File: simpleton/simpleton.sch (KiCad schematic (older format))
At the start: 78 parts

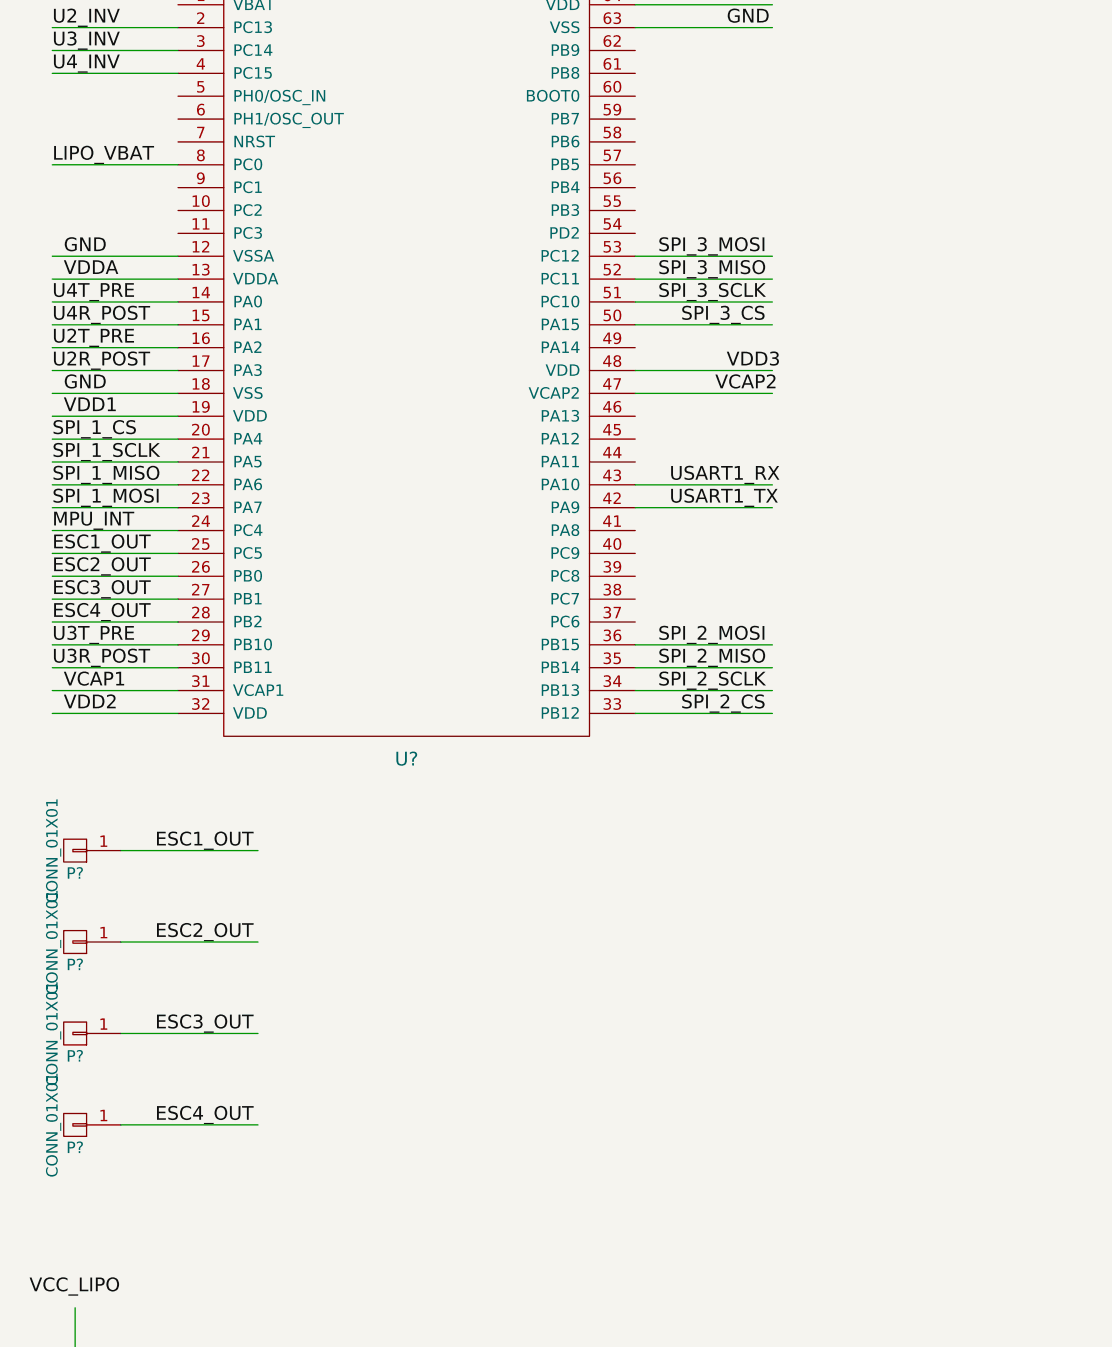
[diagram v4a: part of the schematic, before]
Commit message: Added buzzer
Closes #11
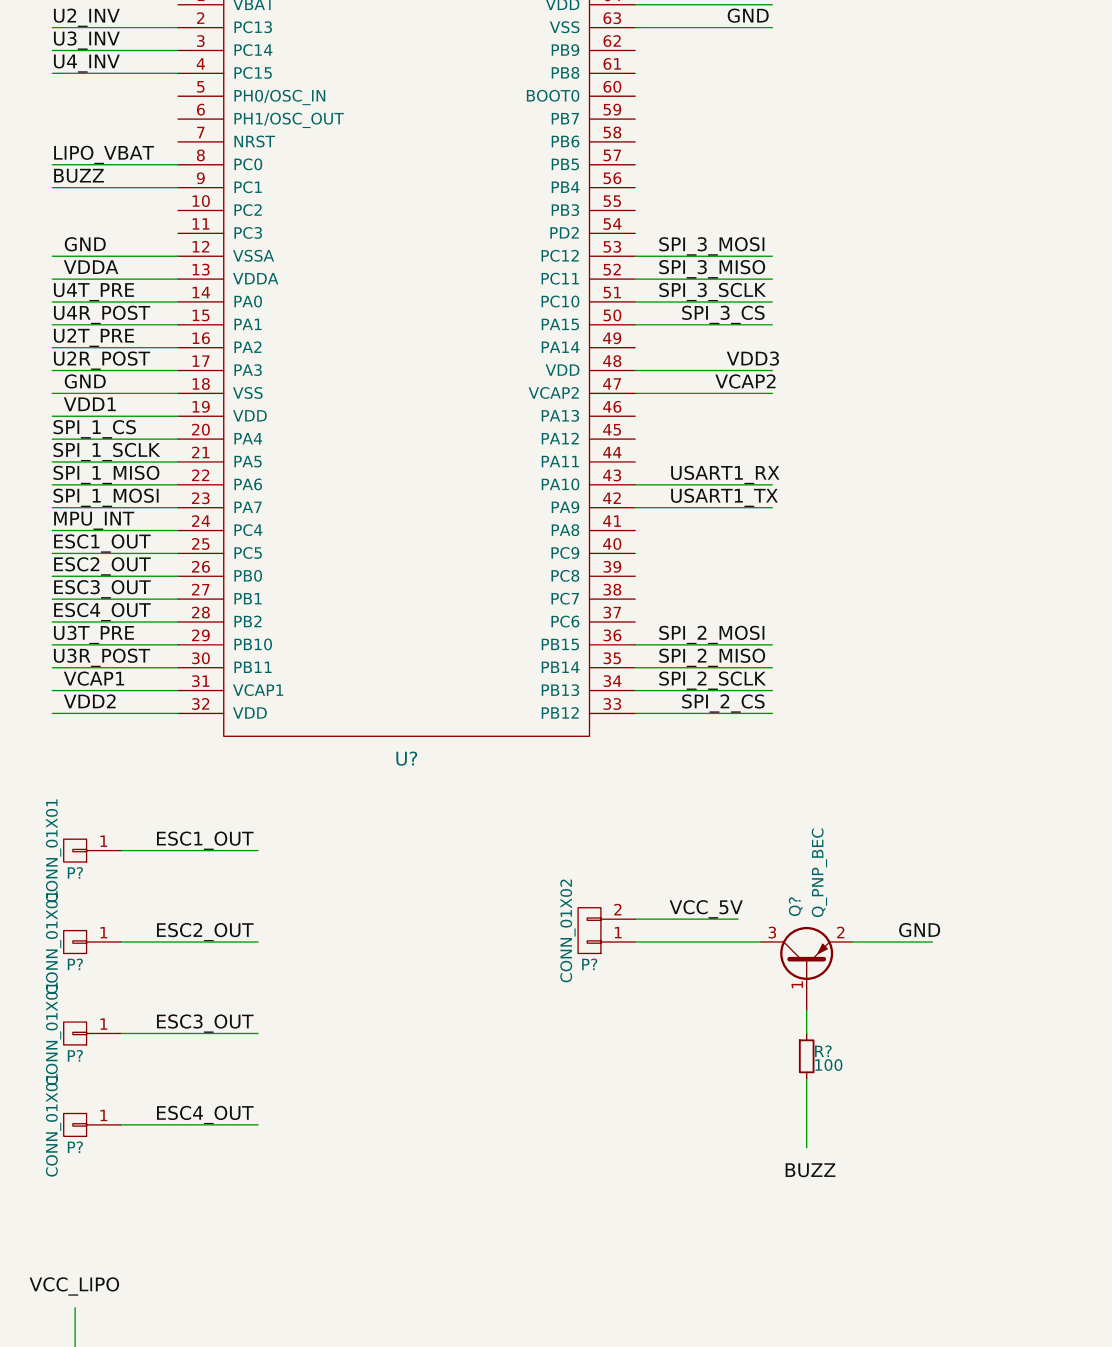
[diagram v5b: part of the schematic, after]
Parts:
- added P?: CONN_01X02, symbol CONN_01X02
- added Q?: Q_PNP_BEC, symbol Q_PNP_BEC
- added R?: 100, symbol R_Small
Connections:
- net labels added: BUZZ
- wire segments 281 -> 287

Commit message: Added status LEDS
Closes #4
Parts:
- added D? (x3): Led_Small, symbol Led_Small
- added R? (x3): 100, symbol R_Small
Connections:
- net labels added: LED1, LED2
- wire segments 287 -> 298
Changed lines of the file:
@@
 Text Label 800  2000 0    60   ~ 0
 BUZZ
+Wire Wire Line
+	2900 6800 2900 7000
+$Comp
+L Led_Small D?
+U 1 1 56D5A53F
+P 2900 7100
+F 0 "D?" H 2850 7225 50  0000 L CNN
+F 1 "Led_Small" H 2725 7000 50  0000 L CNN
+F 2 "" V 2900 7100 60  0000 C CNN
+F 3 "" V 2900 7100 60  0000 C CNN
+	1    2900 7100
+	0    -1   -1   0
+$EndComp
+Wire Wire Line
+	2900 7200 2900 7350
+$Comp
+L R_Small R?
+U 1 1 56D5A97A
+P 2900 7450
+F 0 "R?" H 2930 7470 50  0000 L CNN
+F 1 "100" H 2930 7410 50  0000 L CNN
+F 2 "" H 2900 7450 60  0000 C CNN
+F 3 "" H 2900 7450 60  0000 C CNN
+	1    2900 7450
+	1    0    0    -1
+$EndComp
+Wire Wire Line
+	2900 7550 2900 7700
+Text Label 2800 7800 0    60   ~ 0
+GND
+Text Label 2700 6750 0    60   ~ 0
+VCC_3_3V
+Wire Wire Line
+	3400 6800 3400 7000
+$Comp
+L Led_Small D?
+U 1 1 56D5B127
+P 3400 7100
+F 0 "D?" H 3350 7225 50  0000 L CNN
+F 1 "Led_Small" H 3225 7000 50  0000 L CNN
+F 2 "" V 3400 7100 60  0000 C CNN
+F 3 "" V 3400 7100 60  0000 C CNN
+	1    3400 7100
+	0    -1   -1   0
+$EndComp
+Wire Wire Line
+	3400 7200 3400 7350
+$Comp
+L R_Small R?
+U 1 1 56D5B12E
+P 3400 7450
+F 0 "R?" H 3430 7470 50  0000 L CNN
+F 1 "100" H 3430 7410 50  0000 L CNN
+F 2 "" H 3400 7450 60  0000 C CNN
+F 3 "" H 3400 7450 60  0000 C CNN
+	1    3400 7450
+	1    0    0    -1
+$EndComp
+Wire Wire Line
+	3400 7550 3400 7700
+Text Label 3300 7800 0    60   ~ 0
+LED1
+Text Label 3200 6750 0    60   ~ 0
+VCC_3_3V
+Wire Wire Line
+	3900 6800 3900 7000
+$Comp
+L Led_Small D?
+U 1 1 56D5B212
+P 3900 7100
+F 0 "D?" H 3850 7225 50  0000 L CNN
+F 1 "Led_Small" H 3725 7000 50  0000 L CNN
+F 2 "" V 3900 7100 60  0000 C CNN
+F 3 "" V 3900 7100 60  0000 C CNN
+	1    3900 7100
+	0    -1   -1   0
+$EndComp
+Wire Wire Line
+	3900 7200 3900 7350
+$Comp
+L R_Small R?
+U 1 1 56D5B219
+P 3900 7450
+F 0 "R?" H 3930 7470 50  0000 L CNN
+F 1 "100" H 3930 7410 50  0000 L CNN
+F 2 "" H 3900 7450 60  0000 C CNN
+F 3 "" H 3900 7450 60  0000 C CNN
+	1    3900 7450
+	1    0    0    -1
+$EndComp
+Wire Wire Line
+	3900 7550 3900 7700
+Text Label 3800 7800 0    60   ~ 0
+LED2
+Text Label 3700 6750 0    60   ~ 0
+VCC_3_3V
+Wire Wire Line
+	3350 1900 3950 1900
+Wire Wire Line
+	3350 1800 3950 1800
+Text Label 3750 1900 0    60   ~ 0
+LED1
+Text Label 3750 1800 0    60   ~ 0
+LED2
 $EndSCHEMATC

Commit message: Added boot loader support
Closes #14
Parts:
- added JP?: Jumper_NO_Small, symbol Jumper_NO_Small
- added R?: 10K, symbol R_Small
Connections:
- net labels added: BOOT0
- wire segments 298 -> 304
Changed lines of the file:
@@
 Text Label 1250 6100 0    60   ~ 0
-ESC4_OUT
-Text Label 800  3600 0    60   ~ 0
-ESC1_OUT
-Text Label 800  3700 0    60   ~ 0
-ESC2_OUT
-Text Label 800  3800 0    60   ~ 0
-ESC3_OUT
-Text Label 800  3900 0    60   ~ 0
 ESC4_OUT
 $Comp
@@
 	1100 6100 1700 6100
 Wire Wire Line
-	1350 3600 800  3600
-Wire Wire Line
-	1350 3700 800  3700
-Wire Wire Line
-	1350 3800 800  3800
-Wire Wire Line
 	1350 3900 800  3900
 Wire Wire Line
@@
 Text Label 3750 1800 0    60   ~ 0
 LED2
+Wire Wire Line
+	3350 3900 3950 3900
+Wire Wire Line
+	3350 3800 3950 3800
+Wire Wire Line
+	3350 3700 3950 3700
+Wire Wire Line
+	3350 3600 3950 3600
+Text Label 3500 3900 0    60   ~ 0
+ESC1_OUT
+Text Label 3500 3800 0    60   ~ 0
+ESC2_OUT
+Text Label 3500 3700 0    60   ~ 0
+ESC3_OUT
+Text Label 3500 3600 0    60   ~ 0
+ESC4_OUT
+Text Label 800  3900 0    60   ~ 0
+GND
+Wire Wire Line
+	3350 1600 3950 1600
+Text Label 3650 1600 0    60   ~ 0
+BOOT0
+Wire Wire Line
+	5550 4400 6250 4400
+Wire Wire Line
+	6000 4400 6000 4250
+Connection ~ 6000 4400
+$Comp
+L R_Small R?
+U 1 1 57133C31
+P 6350 4400
+F 0 "R?" H 6380 4420 50  0000 L CNN
+F 1 "10K" H 6380 4360 50  0000 L CNN
+F 2 "" H 6350 4400 60  0000 C CNN
+F 3 "" H 6350 4400 60  0000 C CNN
+	1    6350 4400
+	0    1    1    0
+$EndComp
+Wire Wire Line
+	6450 4400 6800 4400
+Text Label 6650 4400 0    60   ~ 0
+GND
+Text Label 5550 4400 0    60   ~ 0
+BOOT0
+$Comp
+L Jumper_NO_Small JP?
+U 1 1 5713413B
+P 6000 4150
+F 0 "JP?" H 6000 4230 50  0000 C CNN
+F 1 "Jumper_NO_Small" H 6010 4090 50  0001 C CNN
+F 2 "" H 6000 4150 60  0000 C CNN
+F 3 "" H 6000 4150 60  0000 C CNN
+	1    6000 4150
+	0    1    1    0
+$EndComp
+Wire Wire Line
+	6000 4050 6000 3800
+Text Label 5800 3750 0    60   ~ 0
+VCC_3_3V
 $EndSCHEMATC

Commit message: Moved to STM32F3 solution
- Swapped MCU
- Added current sensor
- Increase 3.3V regulator to 500mA version
- Removed UART inverters
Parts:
- removed C?: 22nF, symbol C_Small
- removed C? (x2): 10uF, symbol C_Small
- removed C? (x5): 100nF, symbol C_Small
- removed C? (x3): 1uF, symbol C_Small
- removed C? (x2): 2.2uF, symbol C_Small
- removed C?: 4.7uF, symbol C_Small
- removed C?: 0.1uF, symbol C_Small
- removed D?: Led_Small, symbol Led_Small
- removed P? (x2): CONN_01X02, symbol CONN_01X02
- removed P? (x4): CONN_01X04, symbol CONN_01X04
- removed P?: CONN_01X03, symbol CONN_01X03
- removed P? (x4): CONN_01X01, symbol CONN_01X01
- removed Q?: Q_PNP_BEC, symbol Q_PNP_BEC
- removed R?: 100, symbol R_Small
- removed U?: STM32F405RG, symbol STM32F405RG
- removed U?: RT9193-GB, symbol RT9193-GB
- removed U?: CP2104, symbol CP2104
- removed U? (x3): SN74LVC2G86, symbol SN74LVC2G86
- added C? (x4): 100nF, symbol C_Small
- added C?: 4.7uF, symbol C_Small
- added C?: 10nF, symbol C_Small
- added C? (x3): 1uF, symbol C_Small
- added C? (x2): 20pF, symbol C_Small
- added Q?: Q_NPN_BCE, symbol Q_NPN_BCE
- added R?: 100k, symbol R_Small
- added U?: STM32F303CC, symbol STM32F303CC
- added U?: INA169, symbol INA169
- added U?: RT9013-33GB, symbol RT9013-33GB
- added Y?: 8Mhz, symbol Crystal_Small
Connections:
- net labels added: BUZZ_GND, BUZZ_P, CUR_SENSE, LIPO_N, LIPO_P, OSC_IN, OSC_OUT, UART1_RX, UART1_TX, UART2_RX, UART2_TX, UART3_RX, UART3_TX
- net labels removed: U2R_POST, U2R_PRE, U2T_POST, U2T_PRE, U2_INV, U3R_POST, U3R_PRE, U3T_POST, U3T_PRE, U3_INV, U4R_POST, U4R_PRE, U4T_POST, U4T_PRE, U4_INV, USART1_RX, USART1_TX, VCAP1, VCAP2, VCC_12V, VDD1, VDD2, VDD3, VDD4, VDDA
- wire segments 304 -> 244
- no-connect marks 40 -> 27
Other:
- moved on the sheet: C?, D?, J?, JP?, L?, R?, U?, Y?
